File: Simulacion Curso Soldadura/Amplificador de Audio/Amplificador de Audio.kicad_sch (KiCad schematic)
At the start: 8 parts, among them U1 LM386

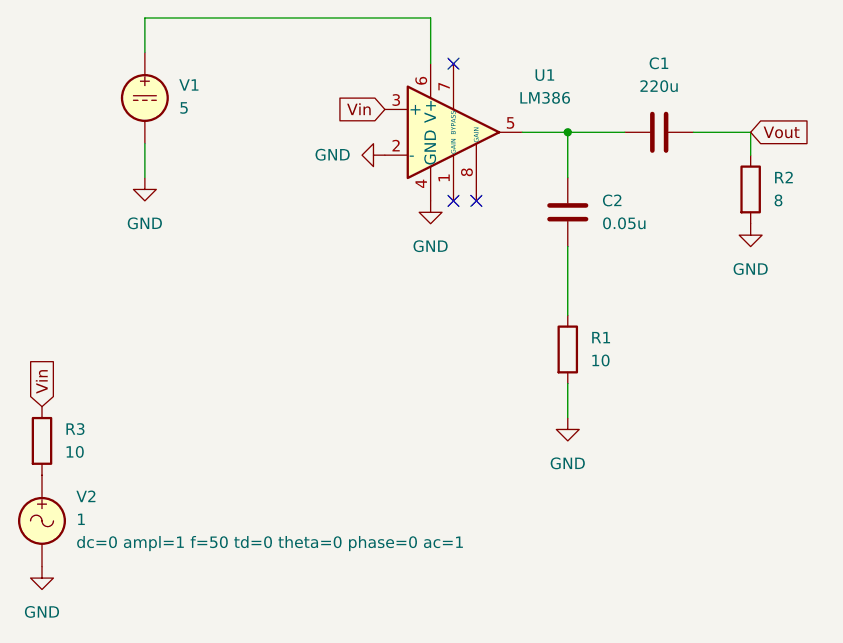
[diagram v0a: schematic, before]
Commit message: Modificacíon simu ampli--OK
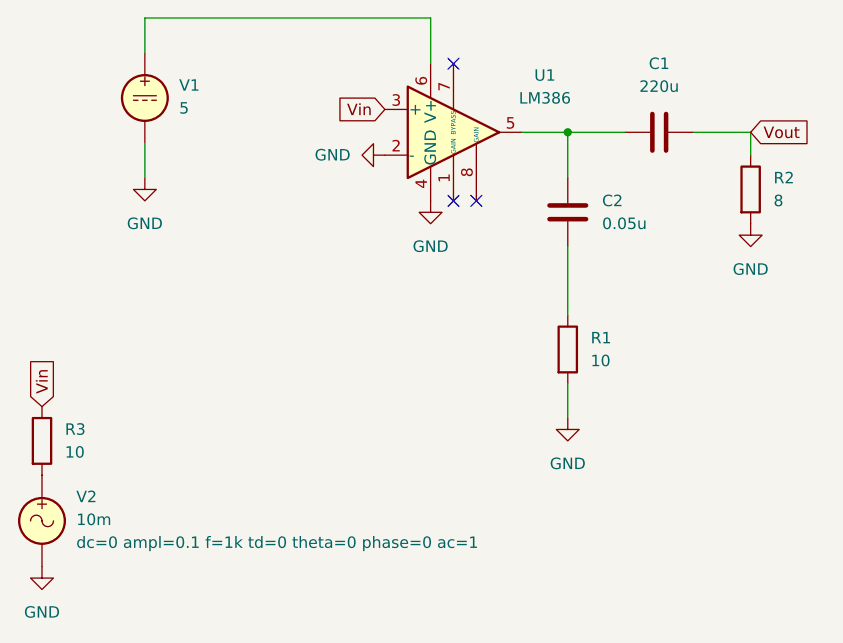
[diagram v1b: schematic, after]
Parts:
- V2: value 1 -> 10m
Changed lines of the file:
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@@
 		)
 		(instances
-			(project ""
+			(project "Amplificador de Audio"
 				(path "/b8d0d51e-a4b5-41db-bca1-70d5e047cb87"
 					(reference "#PWR01")
@@
 		)
 		(instances
-			(project ""
+			(project "Amplificador de Audio"
 				(path "/b8d0d51e-a4b5-41db-bca1-70d5e047cb87"
 					(reference "V1")
@@
 			)
 		)
-		(property "Value" "1"
+		(property "Value" "10m"
 			(at 69.85 125.6001 0)
 			(effects
@@
 			)
 		)
-		(property "Sim.Params" "dc=0 ampl=1 f=50 td=0 theta=0 phase=0 ac=1"
+		(property "Sim.Params" "dc=0 ampl=0.1 f=1k td=0 theta=0 phase=0 ac=1"
 			(at 69.85 128.1401 0)
 			(effects
@@
 		)
 		(instances
-			(project ""
+			(project "Amplificador de Audio"
 				(path "/b8d0d51e-a4b5-41db-bca1-70d5e047cb87"
 					(reference "V2")
@@
 		)
 		(instances
-			(project ""
+			(project "Amplificador de Audio"
 				(path "/b8d0d51e-a4b5-41db-bca1-70d5e047cb87"
 					(reference "R1")
@@
 		)
 		(instances
-			(project ""
+			(project "Amplificador de Audio"
 				(path "/b8d0d51e-a4b5-41db-bca1-70d5e047cb87"
 					(reference "U1")
@@
 		)
 		(instances
-			(project ""
+			(project "Amplificador de Audio"
 				(path "/b8d0d51e-a4b5-41db-bca1-70d5e047cb87"
 					(reference "C1")
